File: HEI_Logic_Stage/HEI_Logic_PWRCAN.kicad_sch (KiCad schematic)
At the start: 28 parts, among them J7 RJ_{1}, J8 RJ_{2}, SW3 SW_SPST, U10 TMH 1212S, U11 B1203XT-1WR3, U12 5V_Converter_R-78E5.0-0.5, U13 5V_Converter_R-78E5.0-0.5, U14 ADM3058EBRIZ

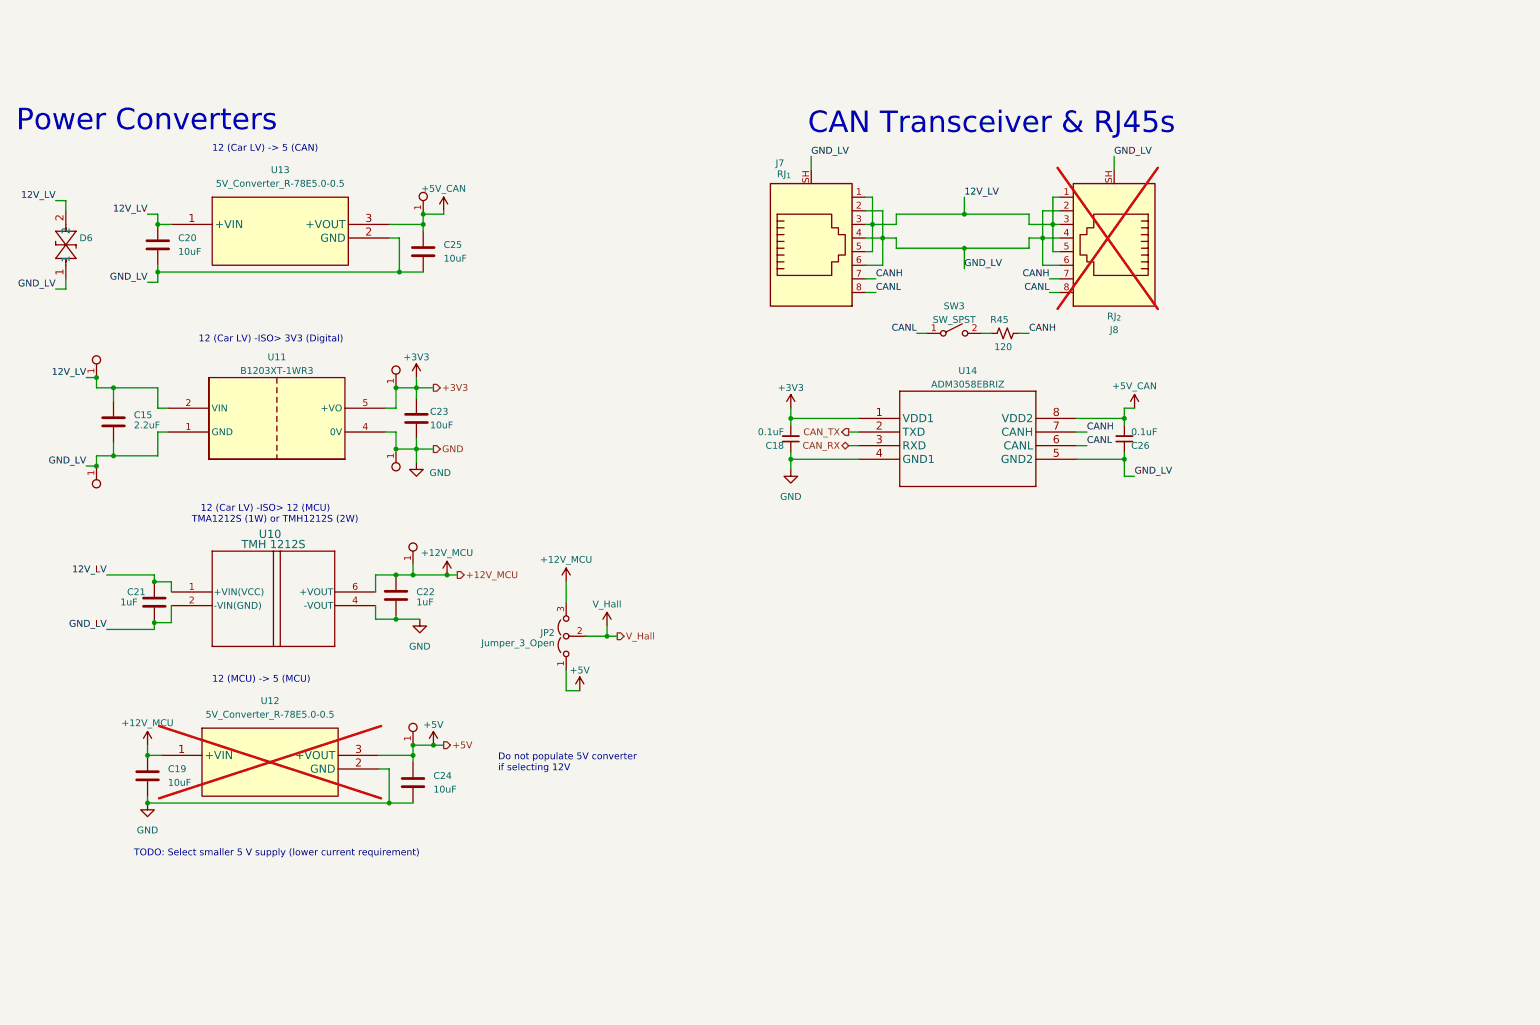
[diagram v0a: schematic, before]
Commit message: new parts into Parts
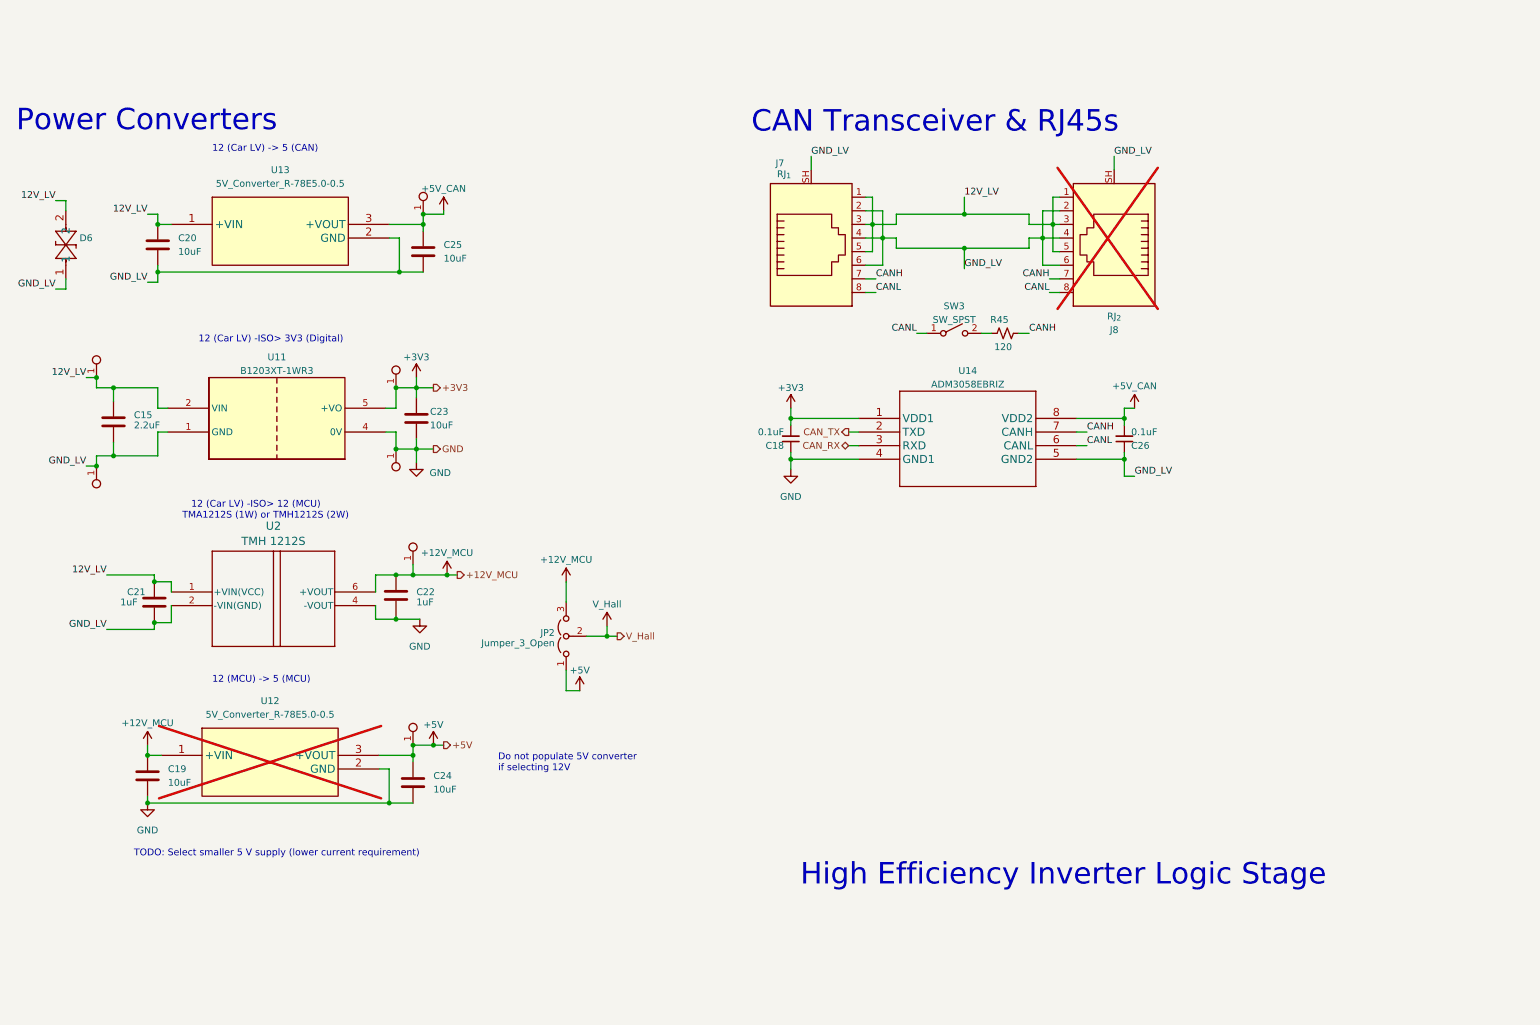
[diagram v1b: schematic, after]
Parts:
- removed U10: TMH 1212S, GTSR_KiCAD_Footprints:TMH SINGLE_TRP, symbol TMH1212S:TMH_1212S
- added U2: TMH 1212S, HEI_Logic:TMH SINGLE_TRP, symbol HEI_Logic:TMH_1212S
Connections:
- net +12V_MCU: now also U2.6 (+VOUT)
- net 12V_LV: now also U2.1 (+VIN(VCC))
- net GND: now also U2.4 (-VOUT)
- net GND_LV: now also U2.2 (-VIN(GND))
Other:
- note added: "High Efficiency Inverter Logic Stage"
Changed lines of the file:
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@@
+		)
+	)
+	(text "High Efficiency Inverter Logic Stage"
+		(exclude_from_sim no)
+		(at 180.848 175.768 0)
+		(effects
+			(font
+				(face "Rockwell")
+				(size 4 4)
+			)
+			(justify left bottom)
 		)
 	)
 	(text "   12 (Car LV) -ISO> 12 (MCU)\nTMA1212S (1W) or TMH1212S (2W)"
 		(exclude_from_sim no)
-		(at 67.31 107.95 0)
+		(at 65.532 107.188 0)
 		(effects
 			(font
@@
 	(text "CAN Transceiver & RJ45s"
 		(exclude_from_sim no)
-		(at 182.245 35.56 0)
+		(at 171.704 35.306 0)
 		(effects
 			(font
@@
 	)
 	(symbol
+		(lib_id "HEI_Logic:TMH_1212S")
+		(at 63.5 120.65 0)
+		(unit 1)
+		(exclude_from_sim no)
+		(in_bom yes)
+		(on_board yes)
+		(dnp no)
+		(fields_autoplaced yes)
+		(property "Reference" "U2"
+			(at 82.55 108.3361 0)
+			(effects
+				(font
+					(size 1.524 1.524)
+				)
+			)
+		)
+		(property "Value" "TMH 1212S"
+			(at 82.55 111.169 0)
+			(effects
+				(font
+					(size 1.524 1.524)
+				)
+			)
+		)
+		(property "Footprint" "HEI_Logic:TMH SINGLE_TRP"
+			(at 63.5 120.65 0)
+			(effects
+				(font
+					(size 1.27 1.27)
+					(italic yes)
+				)
+				(hide yes)
+			)
+		)
+		(property "Datasheet" "https://www.digikey.com/en/products/detail/traco-power/TMH-1212S/9383360"
+			(at 63.5 120.65 0)
+			(effects
+				(font
+					(size 1.27 1.27)
+					(italic yes)
+				)
+				(hide yes)
+			)
+		)
+		(property "Description" ""
+			(at 63.5 120.65 0)
+			(effects
+				(font
+					(size 1.27 1.27)
+				)
+				(hide yes)
+			)
+		)
+		(property "Populate" ""
+			(at 63.5 120.65 0)
+			(effects
+				(font
+					(size 1.27 1.27)
+				)
+			)
+		)
+		(pin "2"
+		)
+		(pin "1"
+		)
+		(pin "6"
+		)
+		(pin "4"
+		)
+		(instances
+			(project ""
+				(path "/9d05e1b7-f292-46e2-9203-5654fb6f820e/0de18315-f7ce-42ca-adfe-a88a58247ef3"
+					(reference "U2")
+					(unit 1)
+				)
+			)
+		)
+	)
+	(symbol
 		(lib_id "Device:C")
 		(at 52.705 88.9 0)
@@
 					(unit 1)
 				)
-			)
-		)
-	)
-	(symbol
-		(lib_id "TMH1212S:TMH_1212S")
-		(at 63.5 120.65 0)
-		(unit 1)
-		(exclude_from_sim no)
-		(in_bom yes)
-		(on_board yes)
-		(dnp no)
-		(property "Reference" "U10"
-			(at 81.915 109.855 0)
-			(effects
-				(font
-					(size 1.524 1.524)
-				)
-			)
-		)
-		(property "Value" "TMH 1212S"
-			(at 82.55 111.76 0)
-			(effects
-				(font
-					(size 1.524 1.524)
-				)
-			)
-		)
-		(property "Footprint" "GTSR_KiCAD_Footprints:TMH SINGLE_TRP"
-			(at 63.5 120.65 0)
-			(effects
-				(font
-					(size 1.27 1.27)
-					(italic yes)
-				)
-				(hide yes)
-			)
-		)
-		(property "Datasheet" "https://www.digikey.com/en/products/detail/traco-power/TMH-1212S/9383360"
-			(at 63.5 120.65 0)
-			(effects
-				(font
-					(size 1.27 1.27)
-					(italic yes)
-				)
-				(hide yes)
-			)
-		)
-		(property "Description" ""
-			(at 63.5 120.65 0)
-			(effects
-				(font
-					(size 1.27 1.27)
-				)
-				(hide yes)
-			)
-		)
-		(property "Populate" ""
-			(at 63.5 120.65 0)
-			(effects
-				(font
-					(size 1.27 1.27)
-				)
-			)
-		)
-		(pin "1"
-		)
-		(pin "2"
-		)
-		(pin "4"
-		)
-		(pin "6"
-		)
-		(instances
-			(project "HEI_Logic"
-				(path "/9d05e1b7-f292-46e2-9203-5654fb6f820e/0de18315-f7ce-42ca-adfe-a88a58247ef3"
-					(reference "U10")
-					(unit 1)
-				)

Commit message: more minor updates
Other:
- note added: "HFI Logic Stage Power & CAN"
- note removed: "High Efficiency Inverter Logic Stage"
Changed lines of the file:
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@@
 		)
 	)
-	(text "High Efficiency Inverter Logic Stage"
+	(text "HFI Logic Stage\nPower & CAN"
 		(exclude_from_sim no)
-		(at 180.848 175.768 0)
+		(at 179.324 180.848 0)
 		(effects
 			(font

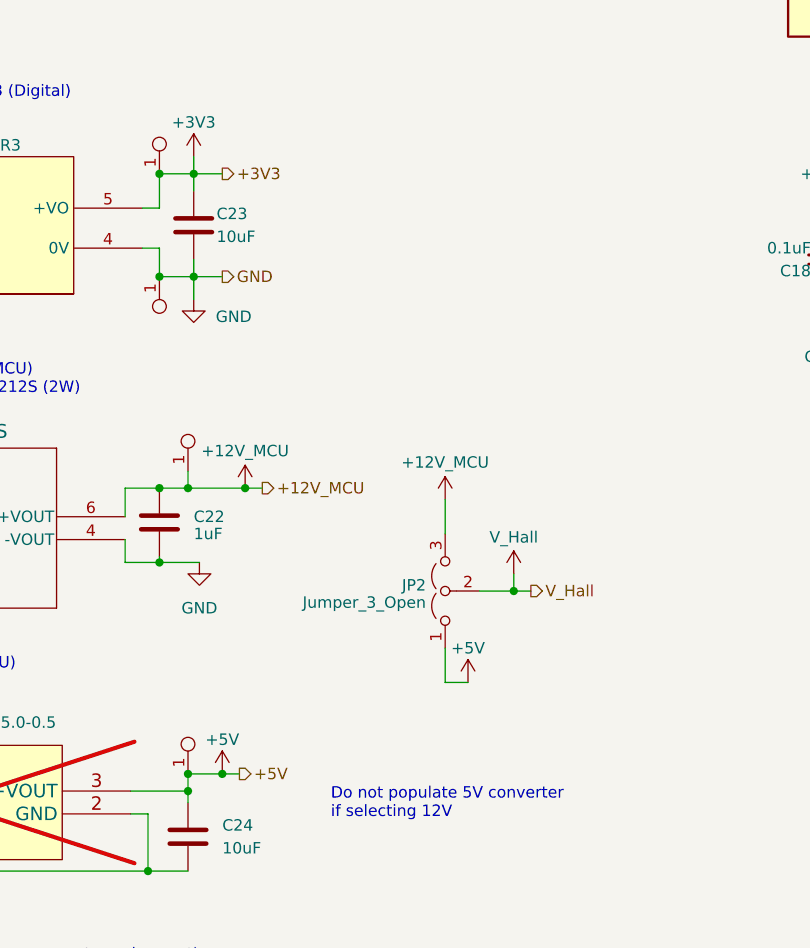
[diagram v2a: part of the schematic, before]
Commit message: fixed logic stage diff amp updates + sim
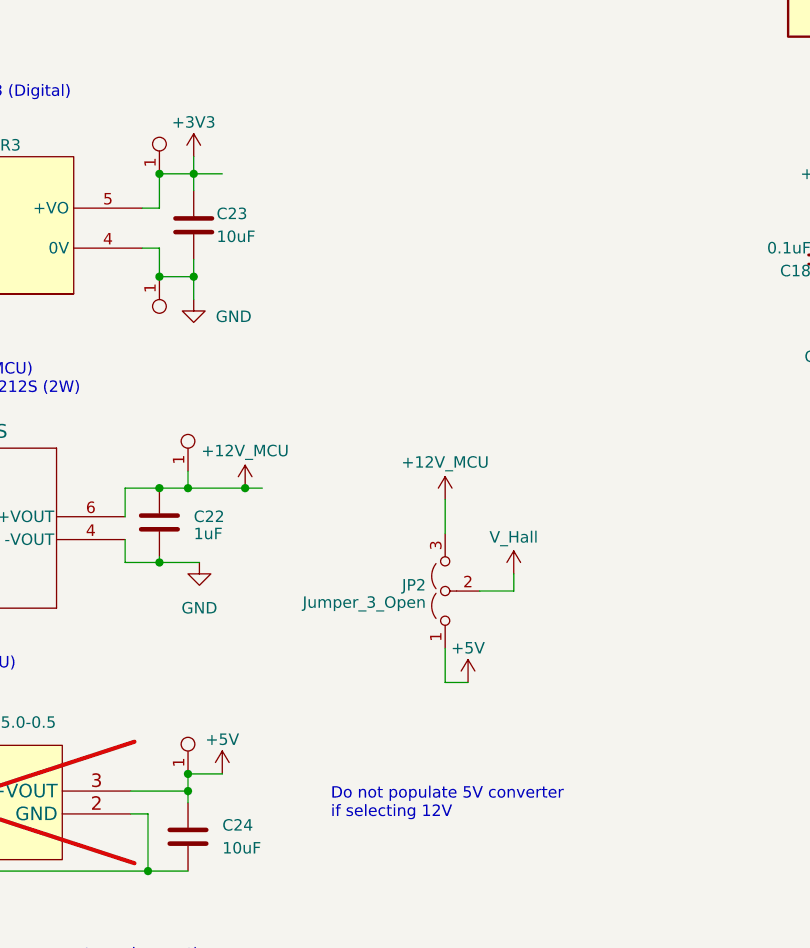
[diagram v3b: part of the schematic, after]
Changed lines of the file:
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@@
-	)
-	(junction
-		(at 112.395 149.225)
-		(diameter 0)
-		(color 0 0 0 0)
 	)
 	(junction
@@
 	)
 	(junction
-		(at 144.78 128.905)
-		(diameter 0)
-		(color 0 0 0 0)
-	)
-	(junction
 		(at 179.07 88.265)
 		(diameter 0)
@@
 	(wire
 		(pts
-			(xy 114.3 149.225) (xy 112.395 149.225)
-		)
-		(stroke
-			(width 0)
-			(type default)
-		)
-	)
-	(wire
-		(pts
 			(xy 196.215 54.61) (xy 196.215 49.53)
 		)
@@
 	(wire
 		(pts
-			(xy 144.78 128.905) (xy 146.685 128.905)
-		)
-		(stroke
-			(width 0)
-			(type default)
-		)
-	)
-	(wire
-		(pts
 			(xy 202.565 72.39) (xy 204.47 72.39)
 		)
@@
 		(pts
 			(xy 41.91 47.625) (xy 43.815 47.625)
-		)
-		(stroke
-			(width 0)
-			(type default)
-		)
-	)
-	(wire
-		(pts
-			(xy 112.395 93.98) (xy 109.22 93.98)
 		)
 		(stroke
@@
 		)
 	)
-	(hierarchical_label "+5V"
-		(shape output)
-		(at 114.3 149.225 0)
-		(fields_autoplaced yes)
-		(effects
-			(font
-				(size 1.27 1.27)
-			)
-			(justify left)
-		)
-	)
 	(hierarchical_label "CAN_TX"
 		(shape output)
@@
 		)
 	)
-	(hierarchical_label "+12V_MCU"
-		(shape output)
-		(at 116.84 117.475 0)
-		(fields_autoplaced yes)
-		(effects
-			(font
-				(size 1.27 1.27)
-			)
-			(justify left)
-		)
-	)
-	(hierarchical_label "V_Hall"
-		(shape output)
-		(at 146.685 128.905 0)
-		(fields_autoplaced yes)
-		(effects
-			(font
-				(size 1.27 1.27)
-			)
-			(justify left)
-		)
-	)
-	(hierarchical_label "GND"
-		(shape output)
-		(at 112.395 93.98 0)
-		(fields_autoplaced yes)
-		(effects
-			(font
-				(size 1.27 1.27)
-			)
-			(justify left)
-		)
-	)
-	(hierarchical_label "+3V3"
-		(shape output)
-		(at 112.395 82.55 0)
-		(fields_autoplaced yes)
-		(effects
-			(font
-				(size 1.27 1.27)
-			)
-			(justify left)
-		)
-	)

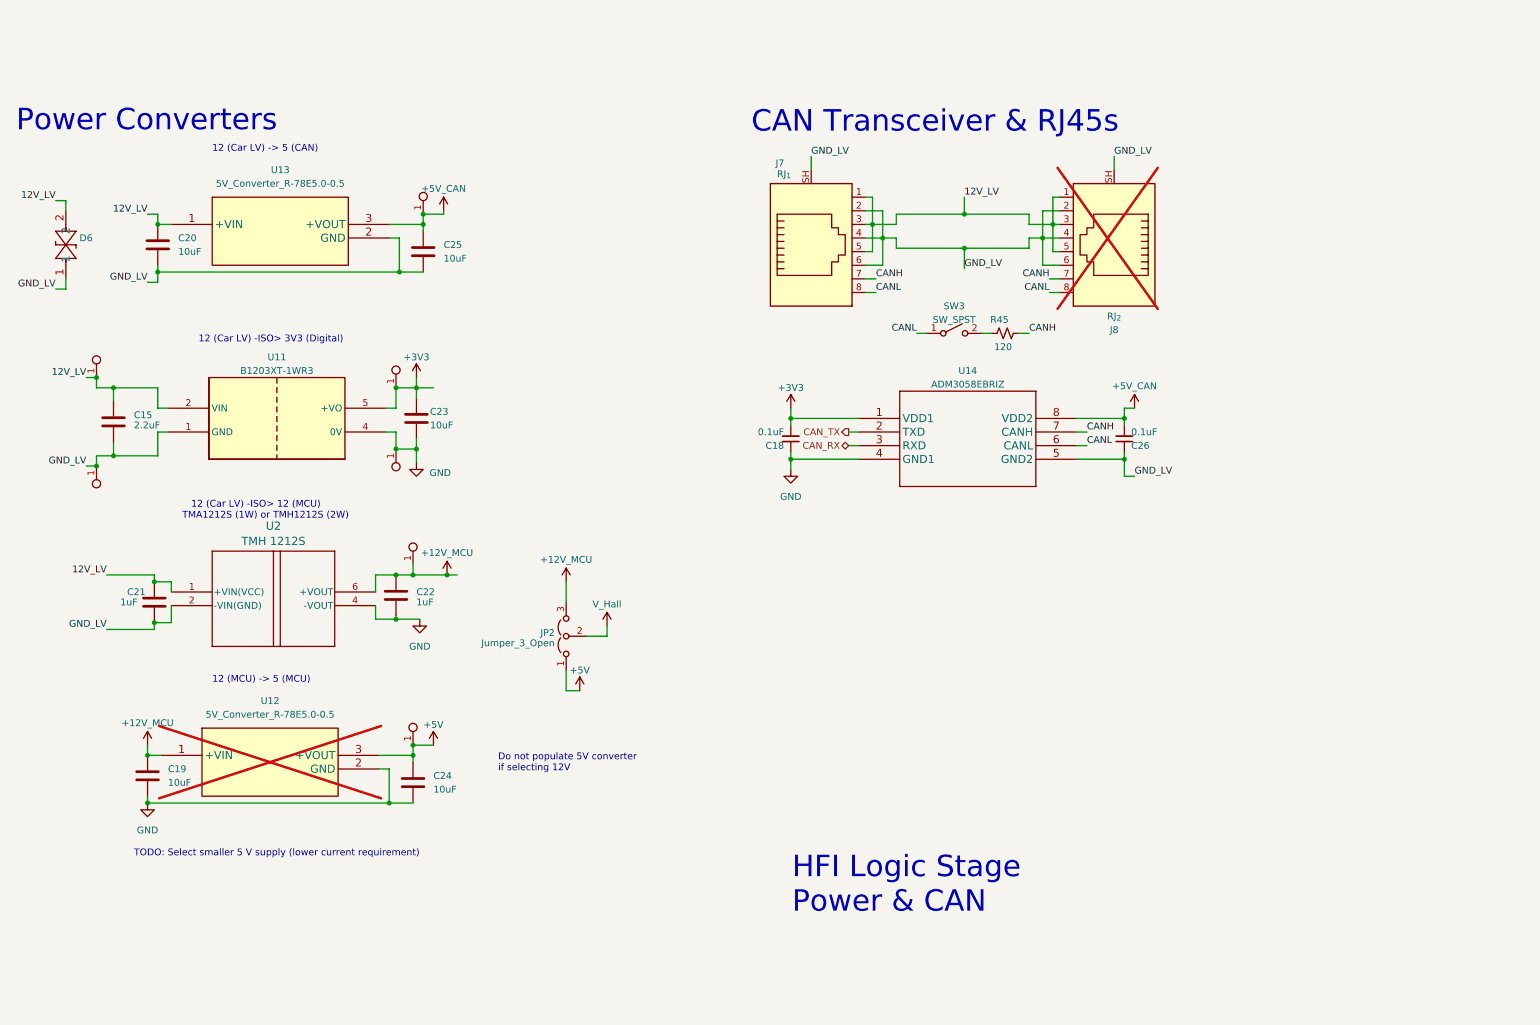
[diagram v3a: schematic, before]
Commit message: vertical logic stage complete
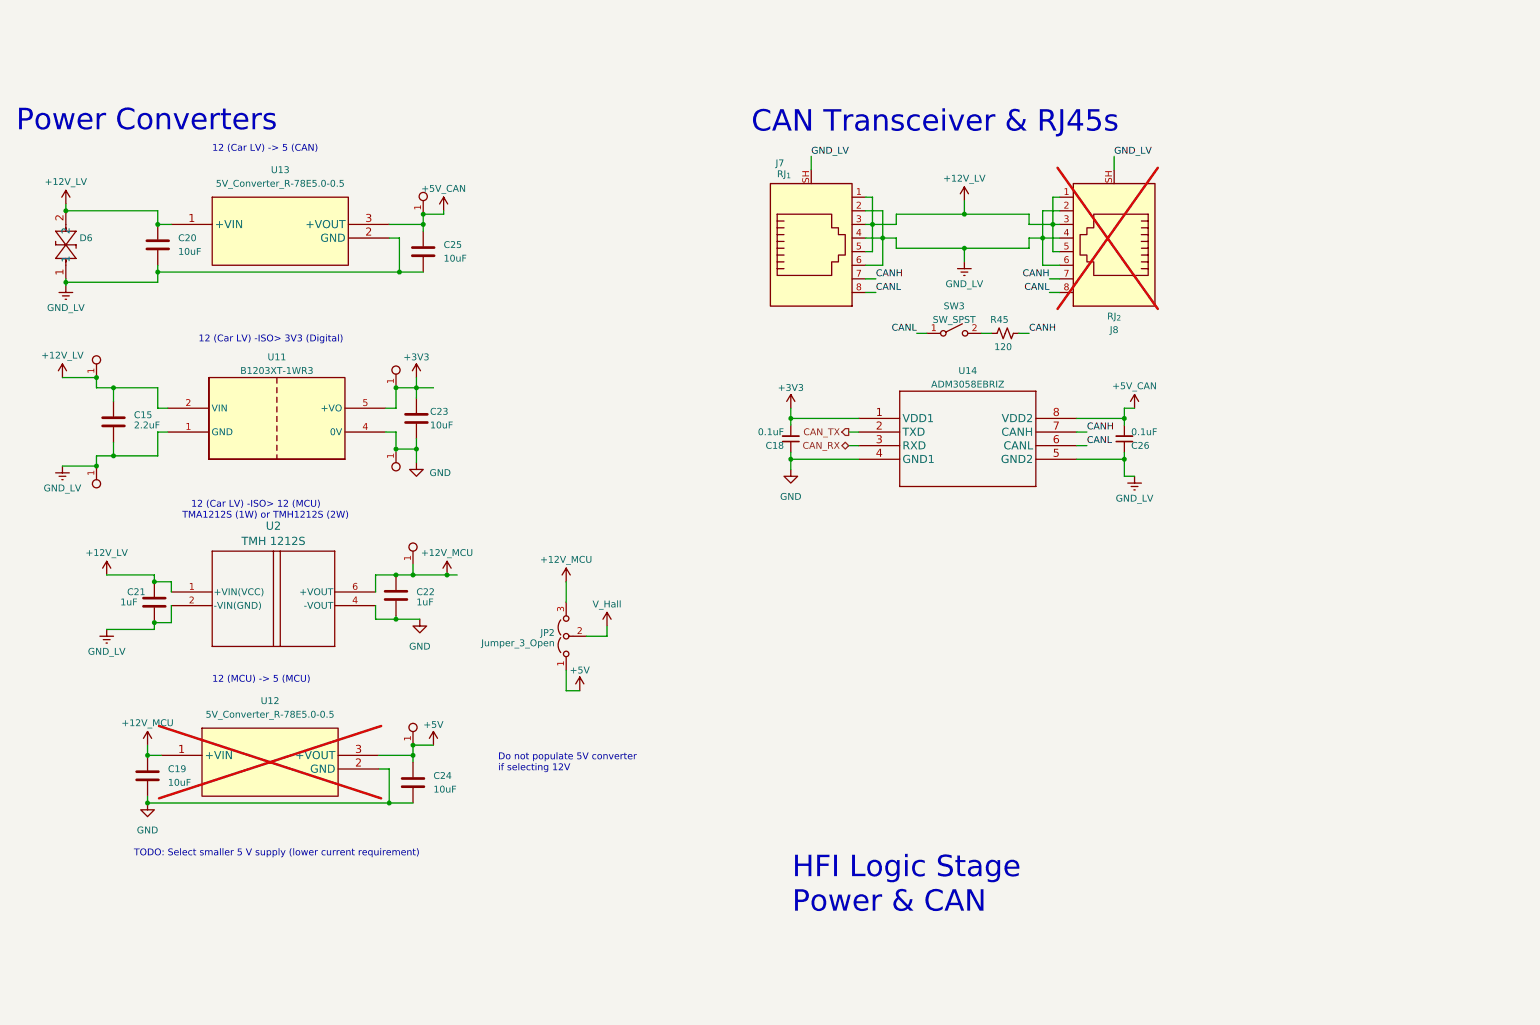
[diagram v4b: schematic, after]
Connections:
- net 12V_LV renamed +12V_LV
